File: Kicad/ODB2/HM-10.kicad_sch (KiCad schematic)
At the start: 0 parts

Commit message: edit titles
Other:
- company: (none) -> GAUL
- title: (none) -> Bluetooth
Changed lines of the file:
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@@
 	(generator_version "8.0")
 	(paper "A4")
+	(title_block
+		(title "Bluetooth")
+		(date "2024-11-09")
+		(company "GAUL")
+	)
 )

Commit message: add titles
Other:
- note added: "Bluetooth"
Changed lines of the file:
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@@
 		(company "GAUL")
 	)
+	(text "Bluetooth"
+		(exclude_from_sim no)
+		(at 34.798 17.78 0)
+		(effects
+			(font
+				(size 6 6)
+				(thickness 1.2)
+				(bold yes)
+			)
+		)
+	)
 )

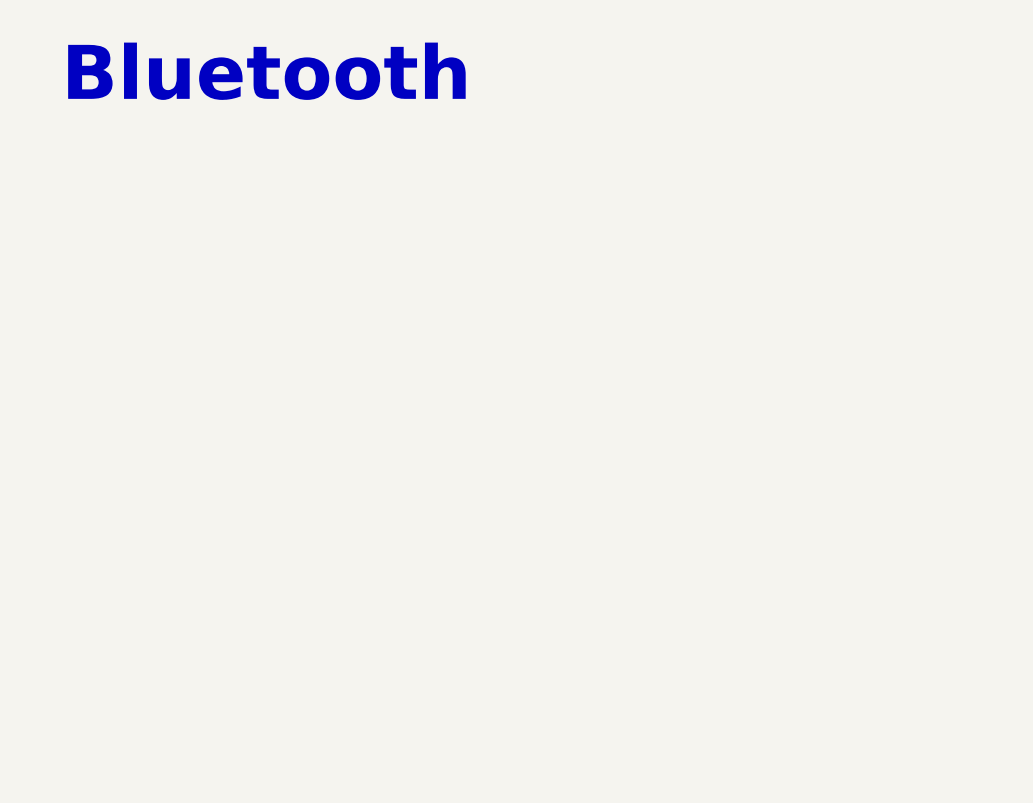
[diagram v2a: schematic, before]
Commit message: add hm10
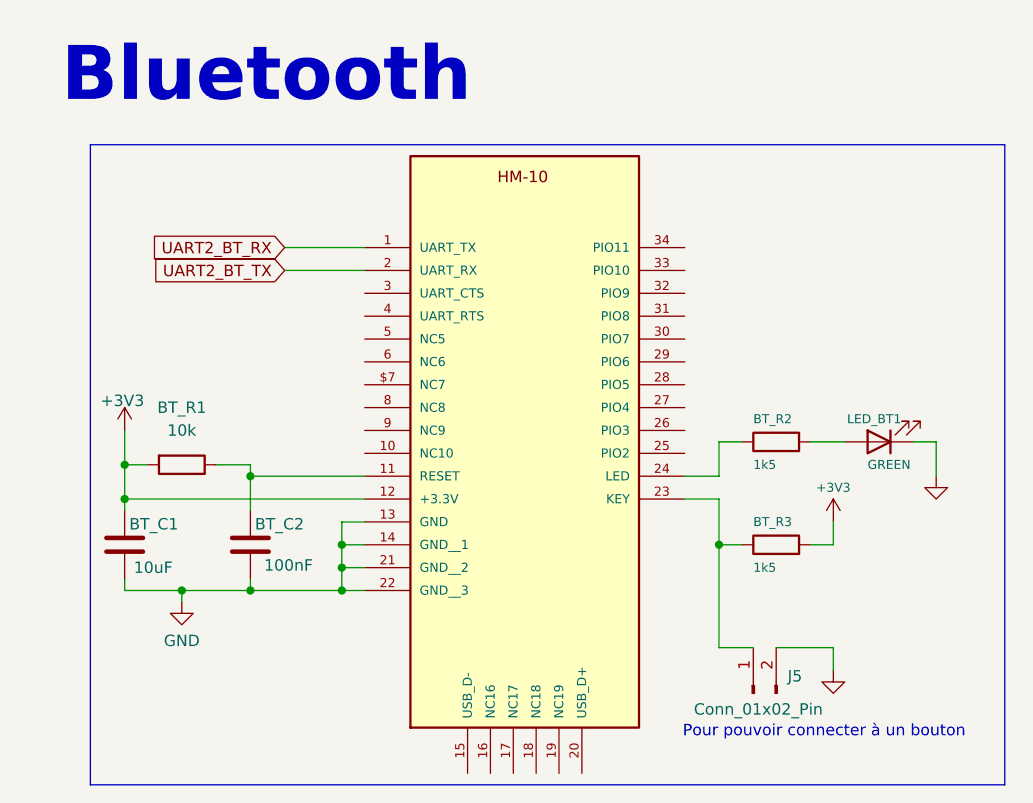
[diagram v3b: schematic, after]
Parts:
- added BT_C1: 10uF, symbol Device:C
- added BT_C2: 100nF, symbol Device:C
- added BT_R1: 10k, symbol Device:R
- added BT_R2, BT_R3: 1k5, Resistor_SMD:R_0805_2012Metric, symbol Device:R
- added E1: HM-10, HM-10:26.9X13X2.2_BOARD, symbol ODB_Lib:HM-10
- added J5: Conn_01x02_Pin, symbol Connector:Conn_01x02_Pin
- added LED_BT1: GREEN, LED_SMD:LED_0805_2012Metric, symbol Device:LED
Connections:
- new net: BT_C2.1, BT_R1.1, E1.11 (RESET)
- new net: BT_R3.1, E1.23 (KEY), J5.1 (Pin_1)
- new net: BT_R2.1, E1.24 (LED)
- new net: BT_R2.2, LED_BT1.2 (A)
- new net +3V3: BT_C1.1, BT_R1.2, BT_R3.2, E1.12 (+3.3V)
- new net GND: BT_C1.2, BT_C2.2, E1.13 (GND), E1.14 (GND__1), E1.21 (GND__2), E1.22 (GND__3), J5.2 (Pin_2), LED_BT1.1 (K)
- new net UART2_BT_RX: E1.1 (UART_TX)
- new net UART2_BT_TX: E1.2 (UART_RX)
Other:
- note added: "Pour pouvoir connecter à un bouton"

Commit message: fix commit
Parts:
- J5: value Conn_01x02_Pin -> BT_Conn_01x02_Pin
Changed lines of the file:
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@@
 			)
 		)
-		(property "Value" "Conn_01x02_Pin"
+		(property "Value" "BT_Conn_01x02_Pin"
 			(at 82.296 88.138 90)
 			(effects

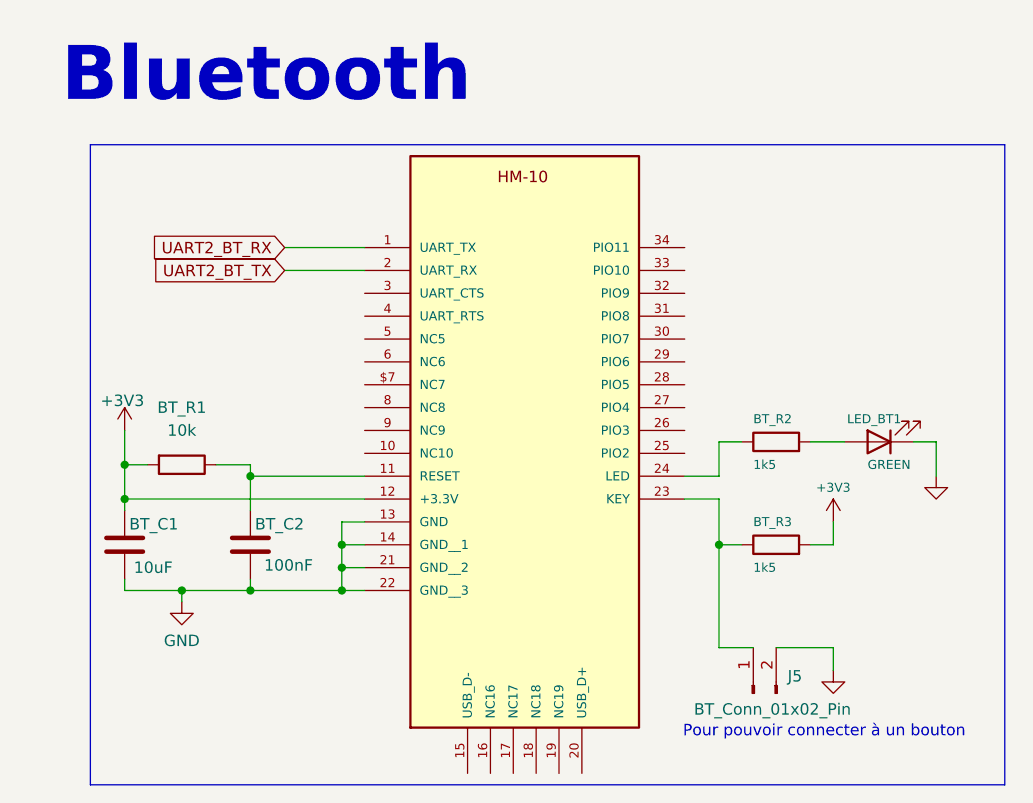
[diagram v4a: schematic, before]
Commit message: add pinout stm32 + fix label
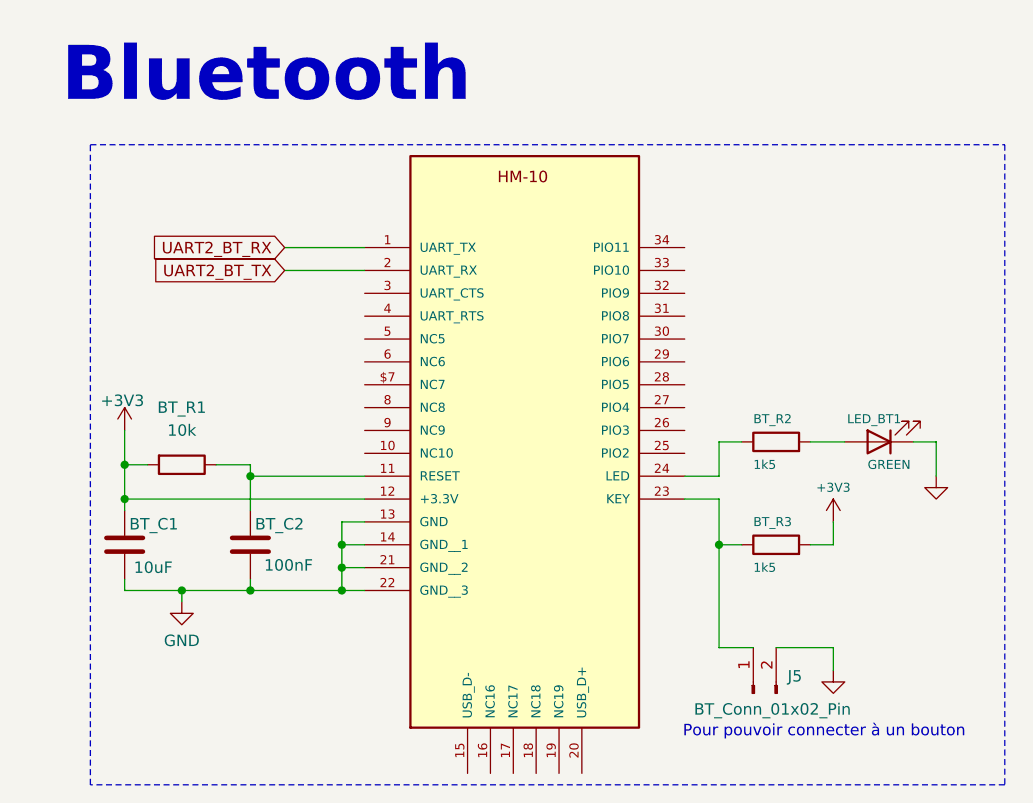
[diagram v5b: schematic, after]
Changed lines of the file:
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@@
 		(stroke
 			(width 0)
-			(type default)
+			(type dash)
 		)
 		(fill

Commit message: fix hm10
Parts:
- removed J5: BT_Conn_01x02_Pin, symbol Connector:Conn_01x02_Pin
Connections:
- net GND: now also BT_R3.1, E1.23 (KEY)
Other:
- note removed: "Pour pouvoir connecter à un bouton"
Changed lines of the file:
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@@
 	(wire
 		(pts
-			(xy 85.09 69.85) (xy 85.09 81.28)
+			(xy 85.09 69.85) (xy 85.09 71.12)
 		)
 		(stroke
@@
 		(pts
 			(xy 85.09 69.85) (xy 87.63 69.85)
-		)
-		(stroke
-			(width 0)
-			(type default)
-		)
-	)
-	(wire
-		(pts
-			(xy 91.44 81.28) (xy 97.79 81.28)
-		)
-		(stroke
-			(width 0)
-			(type default)
-		)
-	)
-	(wire
-		(pts
-			(xy 97.79 81.28) (xy 97.79 83.82)
-		)
-		(stroke
-			(width 0)
-			(type default)
-		)
-	)
-	(wire
-		(pts
-			(xy 85.09 81.28) (xy 88.9 81.28)
 		)
 		(stroke
@@
 				(thickness 1.2)
 				(bold yes)
-			)
-		)
-	)
-	(text "Pour pouvoir connecter à un bouton"
-		(exclude_from_sim no)
-		(at 96.774 90.678 0)
-		(effects
-			(font
-				(size 1.27 1.27)
 			)
 		)
@@
 	)
 	(symbol
-		(lib_id "Connector:Conn_01x02_Pin")
-		(at 88.9 86.36 90)
-		(unit 1)
-		(exclude_from_sim no)
-		(in_bom yes)
-		(on_board yes)
-		(dnp no)
-		(property "Reference" "J5"
-			(at 92.71 84.4549 90)
-			(effects
-				(font
-					(size 1.27 1.27)
-				)
-				(justify right)
-			)
-		)
-		(property "Value" "BT_Conn_01x02_Pin"
-			(at 82.296 88.138 90)
-			(effects
-				(font
-					(size 1.27 1.27)
-				)
-				(justify right)
-			)
-		)
-		(property "Footprint" ""
-			(at 88.9 86.36 0)
-			(effects
-				(font
-					(size 1.27 1.27)
-				)
-				(hide yes)
-			)
-		)
-		(property "Datasheet" "~"
-			(at 88.9 86.36 0)
-			(effects
-				(font
-					(size 1.27 1.27)
-				)
-				(hide yes)
-			)
-		)
-		(property "Description" "Generic connector, single row, 01x02, script generated"
-			(at 88.9 86.36 0)
-			(effects
-				(font
-					(size 1.27 1.27)
-				)
-				(hide yes)
-			)
-		)
-		(pin "1"
-		)
-		(pin "2"
-		)
-		(instances
-			(project "ODB2"
-				(path "/4b06c5d1-aa8b-48ed-8972-b43a60cfab78/eac5f07f-d6a3-4c95-b286-7cebf46e30db/fde591df-8db1-4658-bb0c-169e0f50af3c"
-					(reference "J5")
-					(unit 1)
-				)
-			)
-		)
-	)
-	(symbol
 		(lib_id "power:+3V3")
 		(at 97.79 67.31 0)
@@
 	(symbol
 		(lib_id "power:GND")
-		(at 97.79 83.82 0)
+		(at 85.09 71.12 0)
 		(unit 1)
 		(exclude_from_sim no)
@@
 		(fields_autoplaced yes)
 		(property "Reference" "#PWR065"
-			(at 97.79 90.17 0)
+			(at 85.09 77.47 0)
 			(effects
 				(font
@@
 		)
 		(property "Value" "GND"
-			(at 97.79 88.9 0)
+			(at 85.09 76.2 0)
 			(effects
 				(font
@@
 		)
 		(property "Footprint" ""
-			(at 97.79 83.82 0)
+			(at 85.09 71.12 0)
 			(effects
 				(font
@@
 		)
 		(property "Datasheet" ""
-			(at 97.79 83.82 0)
+			(at 85.09 71.12 0)
 			(effects
 				(font
@@
 		)
 		(property "Description" ""
-			(at 97.79 83.82 0)
-			(effects
-				(font
+			(at 85.09 71.12 0)
+			(effects
+				(font

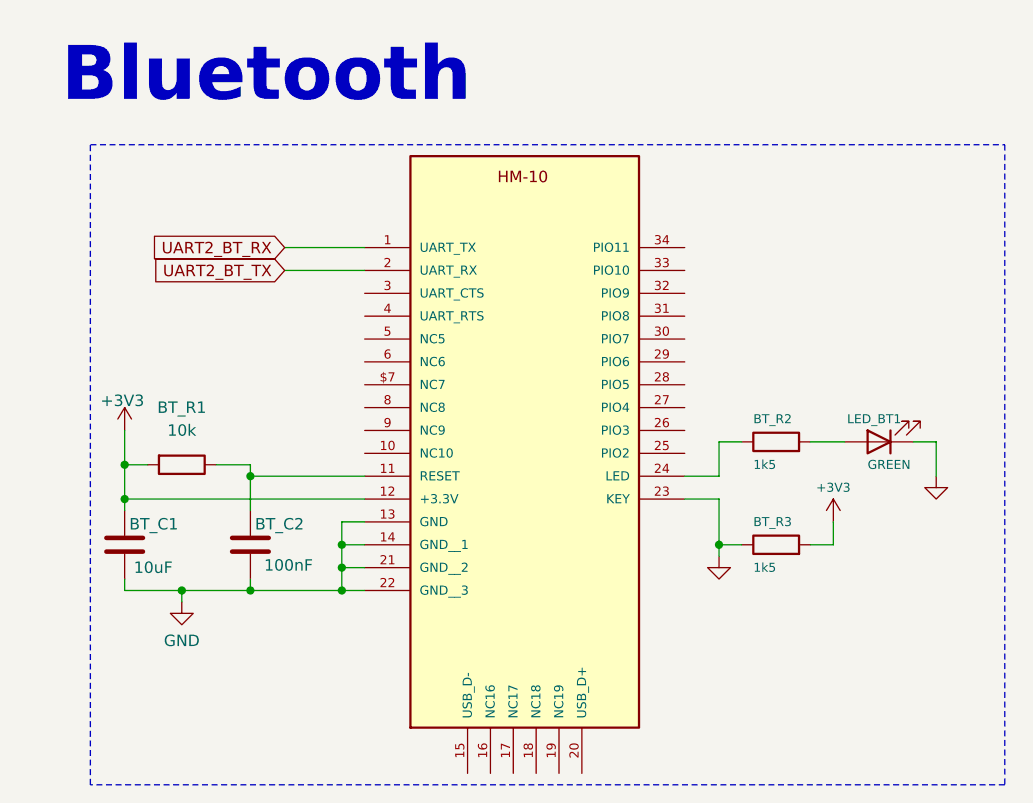
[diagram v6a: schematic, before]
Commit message: merge all sensors to main page + fix NC
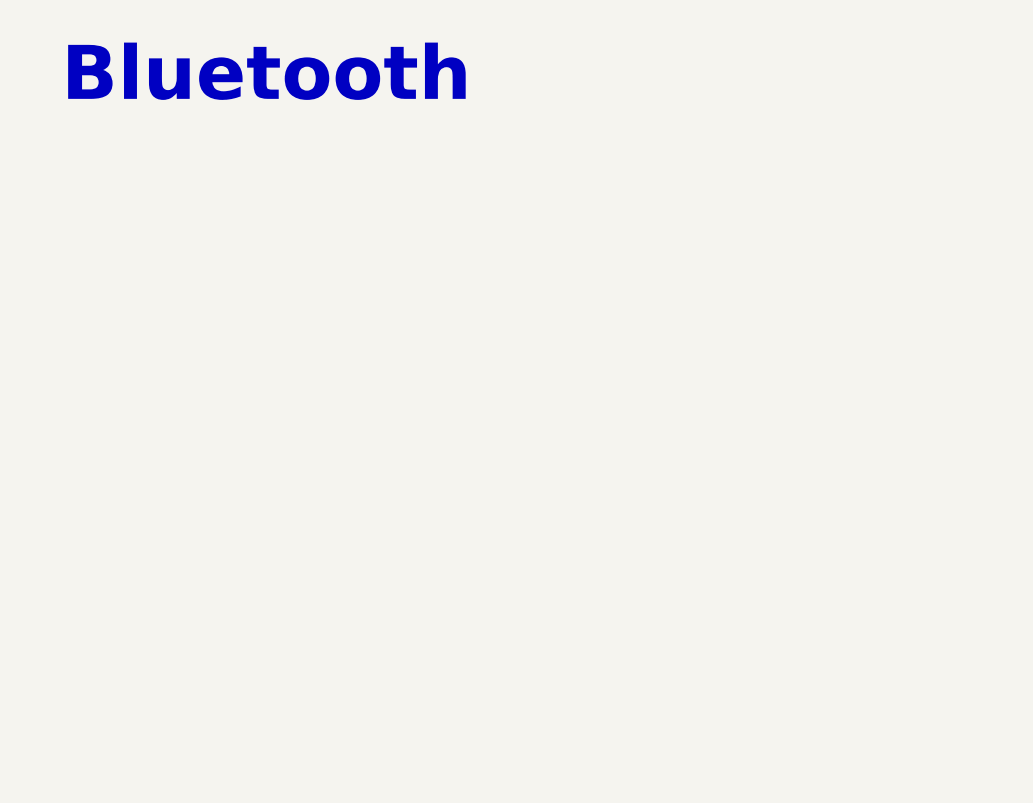
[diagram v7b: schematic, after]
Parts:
- removed BT_C1: 10uF, symbol Device:C
- removed BT_C2: 100nF, symbol Device:C
- removed BT_R1: 10k, symbol Device:R
- removed BT_R2, BT_R3: 1k5, Resistor_SMD:R_0805_2012Metric, symbol Device:R
- removed E1: HM-10, HM-10:26.9X13X2.2_BOARD, symbol ODB_Lib:HM-10
- removed LED_BT1: GREEN, LED_SMD:LED_0805_2012Metric, symbol Device:LED
